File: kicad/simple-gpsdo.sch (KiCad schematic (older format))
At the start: 89 parts, among them J1 PPS_OUT, J2 PWR, J3 ISP, J6 USB_B_Micro, J7 NEO-6M, J8 10MHz_OUT, Q1 DMP3099L, SW1 RST, U1 BD50FC0FP-E2, U2 ATmega32U4-AU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

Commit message: Updated tantalum footprints, started new BOM
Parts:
- C27, C8: footprint Capacitor_SMD:C_1206_3216Metric_Pad1.42x1.75mm_HandSolder -> Capacitor_Tantalum_SMD:CP_EIA-6032-20_AVX-F_Pad2.25x2.35mm_HandSolder
- C3, C32, C34, C35: footprint Capacitor_SMD:C_1206_3216Metric_Pad1.42x1.75mm_HandSolder -> Capacitor_Tantalum_SMD:CP_EIA-3528-15_AVX-H_Pad1.50x2.35mm_HandSolder
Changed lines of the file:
@@
 F 0 "C35" H 8988 5196 50  0000 L CNN
 F 1 "10uF" H 8988 5105 50  0000 L CNN
-F 2 "Capacitor_SMD:C_1206_3216Metric_Pad1.42x1.75mm_HandSolder" H 8900 5150 50  0001 C CNN
+F 2 "Capacitor_Tantalum_SMD:CP_EIA-3528-15_AVX-H_Pad1.50x2.35mm_HandSolder" H 8900 5150 50  0001 C CNN
 F 3 "~" H 8900 5150 50  0001 C CNN
 	1    8900 5150
@@
 F 0 "C34" H 5038 4446 50  0000 L CNN
 F 1 "10uF" H 5038 4355 50  0000 L CNN
-F 2 "Capacitor_SMD:C_1206_3216Metric_Pad1.42x1.75mm_HandSolder" H 4950 4400 50  0001 C CNN
+F 2 "Capacitor_Tantalum_SMD:CP_EIA-3528-15_AVX-H_Pad1.50x2.35mm_HandSolder" H 4950 4400 50  0001 C CNN
 F 3 "~" H 4950 4400 50  0001 C CNN
 	1    4950 4400
@@
 F 0 "C3" H 2588 6996 50  0000 L CNN
 F 1 "10uF" H 2588 6905 50  0000 L CNN
-F 2 "Capacitor_SMD:C_1206_3216Metric_Pad1.42x1.75mm_HandSolder" H 2500 6950 50  0001 C CNN
+F 2 "Capacitor_Tantalum_SMD:CP_EIA-3528-15_AVX-H_Pad1.50x2.35mm_HandSolder" H 2500 6950 50  0001 C CNN
 F 3 "~" H 2500 6950 50  0001 C CNN
 	1    2500 6950
@@
 F 0 "C8" H 4088 7396 50  0000 L CNN
 F 1 "22uF" H 4088 7305 50  0000 L CNN
-F 2 "Capacitor_SMD:C_1206_3216Metric_Pad1.42x1.75mm_HandSolder" H 4000 7350 50  0001 C CNN
+F 2 "Capacitor_Tantalum_SMD:CP_EIA-6032-20_AVX-F_Pad2.25x2.35mm_HandSolder" H 4000 7350 50  0001 C CNN
 F 3 "~" H 4000 7350 50  0001 C CNN
 	1    4000 7350
@@
 F 0 "C27" H 4238 7396 50  0000 L CNN
 F 1 "22uF" H 4238 7305 50  0000 L CNN
-F 2 "Capacitor_SMD:C_1206_3216Metric_Pad1.42x1.75mm_HandSolder" H 4150 7350 50  0001 C CNN
+F 2 "Capacitor_Tantalum_SMD:CP_EIA-6032-20_AVX-F_Pad2.25x2.35mm_HandSolder" H 4150 7350 50  0001 C CNN
 F 3 "~" H 4150 7350 50  0001 C CNN
 	1    4150 7350
@@
 F 0 "C32" H 4638 7396 50  0000 L CNN
 F 1 "10uF" H 4638 7305 50  0000 L CNN
-F 2 "Capacitor_SMD:C_1206_3216Metric_Pad1.42x1.75mm_HandSolder" H 4550 7350 50  0001 C CNN
+F 2 "Capacitor_Tantalum_SMD:CP_EIA-3528-15_AVX-H_Pad1.50x2.35mm_HandSolder" H 4550 7350 50  0001 C CNN
 F 3 "~" H 4550 7350 50  0001 C CNN
 	1    4550 7350

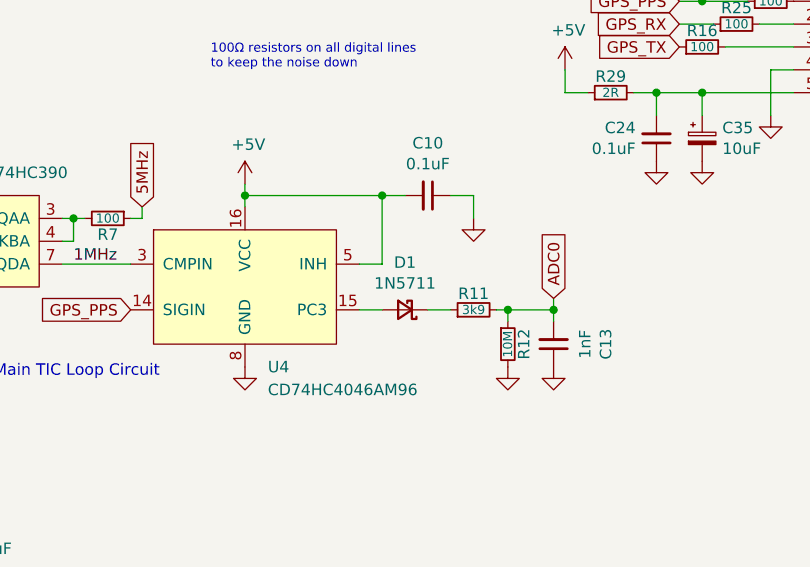
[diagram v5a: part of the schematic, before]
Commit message: Changed 1N5711 to 1N6263 for availability
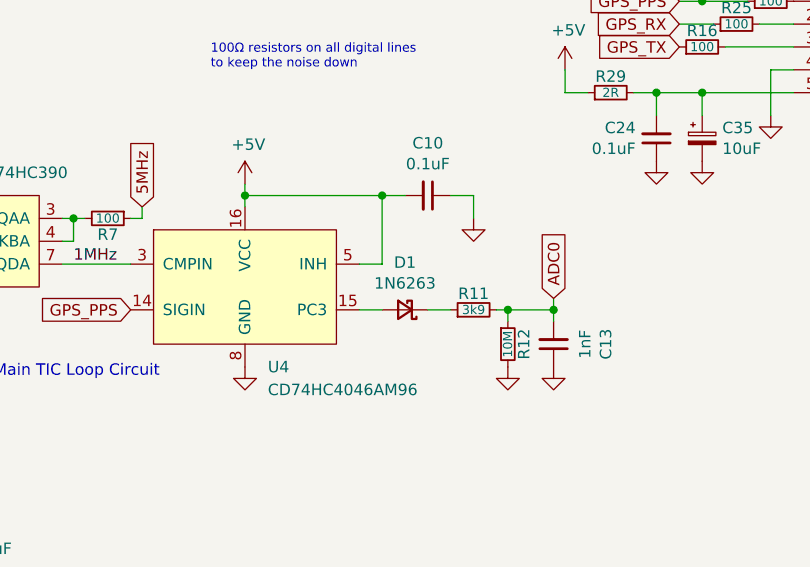
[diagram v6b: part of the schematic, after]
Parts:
- D1: value 1N5711 -> 1N6263
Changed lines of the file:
@@
 P 7600 5900
 F 0 "D1" H 7600 5693 50  0000 C CNN
-F 1 "1N5711" H 7600 5784 50  0000 C CNN
+F 1 "1N6263" H 7600 5784 50  0000 C CNN
 F 2 "Diode_SMD:D_SOD-123" V 7600 5900 50  0001 C CNN
 F 3 "~" V 7600 5900 50  0001 C CNN

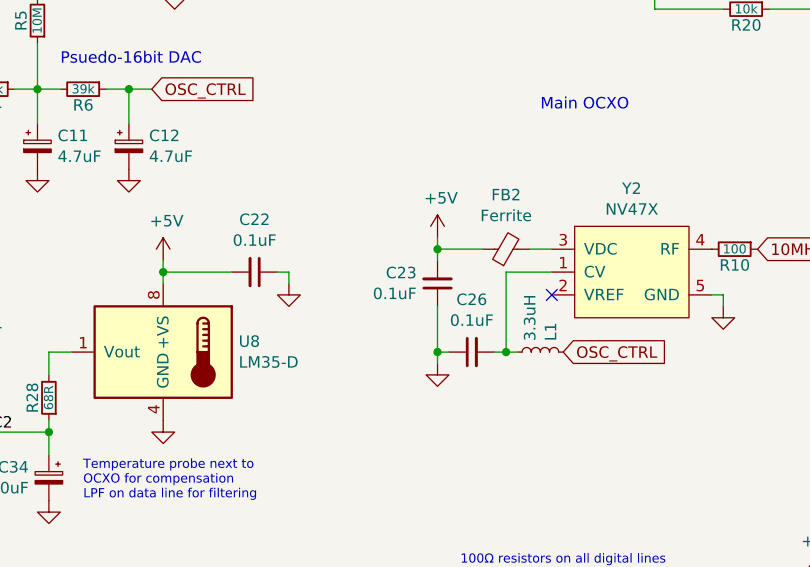
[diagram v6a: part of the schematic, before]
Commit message: Replaced C23 (0.1uF) with C14 (4.7uF)
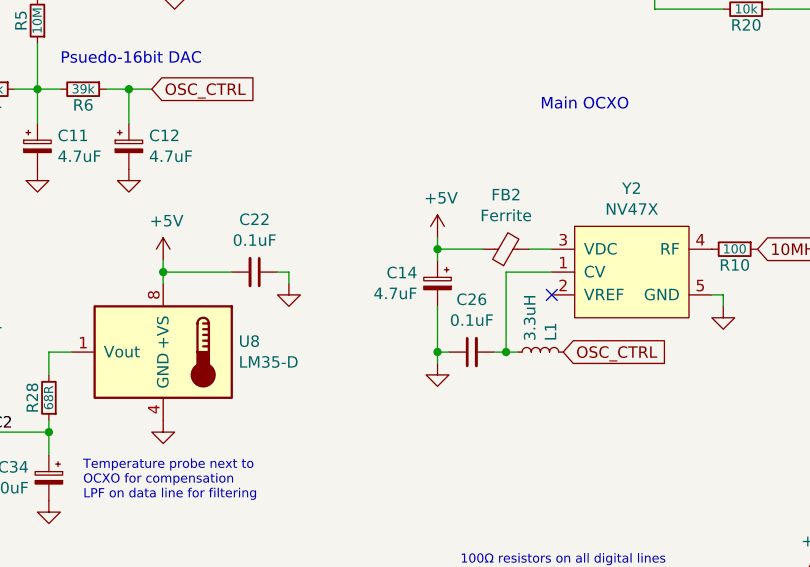
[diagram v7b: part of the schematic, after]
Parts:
- removed C23: 0.1uF, Capacitor_SMD:C_0805_2012Metric_Pad1.15x1.40mm_HandSolder, symbol Device:C_Small
- added C14: 4.7uF, Capacitor_Tantalum_SMD:CP_EIA-3216-10_Kemet-I_Pad1.58x1.35mm_HandSolder, symbol Device:CP_Small
- C11, C12, C25, C30: footprint Capacitor_SMD:C_1206_3216Metric_Pad1.42x1.75mm_HandSolder -> Capacitor_Tantalum_SMD:CP_EIA-3216-10_Kemet-I_Pad1.58x1.35mm_HandSolder
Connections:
- net +5V: now also C14.1
- net GND: now also C14.2
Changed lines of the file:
@@
 F 0 "C11" H 4988 2996 50  0000 L CNN
 F 1 "4.7uF" H 4988 2905 50  0000 L CNN
-F 2 "Capacitor_SMD:C_1206_3216Metric_Pad1.42x1.75mm_HandSolder" H 4900 2950 50  0001 C CNN
+F 2 "Capacitor_Tantalum_SMD:CP_EIA-3216-10_Kemet-I_Pad1.58x1.35mm_HandSolder" H 4900 2950 50  0001 C CNN
 F 3 "~" H 4900 2950 50  0001 C CNN
 	1    4900 2950
@@
 F 0 "C12" H 5388 2996 50  0000 L CNN
 F 1 "4.7uF" H 5388 2905 50  0000 L CNN
-F 2 "Capacitor_SMD:C_1206_3216Metric_Pad1.42x1.75mm_HandSolder" H 5300 2950 50  0001 C CNN
+F 2 "Capacitor_Tantalum_SMD:CP_EIA-3216-10_Kemet-I_Pad1.58x1.35mm_HandSolder" H 5300 2950 50  0001 C CNN
 F 3 "~" H 5300 2950 50  0001 C CNN
 	1    5300 2950
@@
 F 0 "C25" H 1638 1396 50  0000 L CNN
 F 1 "4.7uF" H 1638 1305 50  0000 L CNN
-F 2 "Capacitor_SMD:C_1206_3216Metric_Pad1.42x1.75mm_HandSolder" H 1550 1350 50  0001 C CNN
+F 2 "Capacitor_Tantalum_SMD:CP_EIA-3216-10_Kemet-I_Pad1.58x1.35mm_HandSolder" H 1550 1350 50  0001 C CNN
 F 3 "~" H 1550 1350 50  0001 C CNN
 	1    1550 1350
@@
 OSC_CTRL
 $Comp
-L Device:C_Small C23
-U 1 1 5F6CD16E
-P 6650 3550
-F 0 "C23" H 6559 3504 50  0000 R CNN
-F 1 "0.1uF" H 6559 3595 50  0000 R CNN
-F 2 "Capacitor_SMD:C_0805_2012Metric_Pad1.15x1.40mm_HandSolder" H 6650 3550 50  0001 C CNN
-F 3 "~" H 6650 3550 50  0001 C CNN
-	1    6650 3550
-	1    0    0    1
-$EndComp
-$Comp
 L power:+5V #PWR018
 U 1 1 6199610A
@@
 F 0 "C30" H 5688 6946 50  0000 L CNN
 F 1 "4.7uF" H 5688 6855 50  0000 L CNN
-F 2 "Capacitor_SMD:C_1206_3216Metric_Pad1.42x1.75mm_HandSolder" H 5600 6900 50  0001 C CNN
+F 2 "Capacitor_Tantalum_SMD:CP_EIA-3216-10_Kemet-I_Pad1.58x1.35mm_HandSolder" H 5600 6900 50  0001 C CNN
 F 3 "~" H 5600 6900 50  0001 C CNN
 	1    5600 6900
@@
 Text Notes 8850 3050 0    40   ~ 0
 PPS connection is a jumper\nto bulkhead SMA
+$Comp
+L Device:CP_Small C14
+U 1 1 61775BC3
+P 6650 3550
+F 0 "C14" H 6738 3596 50  0000 L CNN
+F 1 "4.7uF" H 6738 3505 50  0000 L CNN
+F 2 "Capacitor_Tantalum_SMD:CP_EIA-3216-10_Kemet-I_Pad1.58x1.35mm_HandSolder" H 6650 3550 50  0001 C CNN
+F 3 "~" H 6650 3550 50  0001 C CNN
+	1    6650 3550
+	-1   0    0    -1
+$EndComp
 $EndSCHEMATC

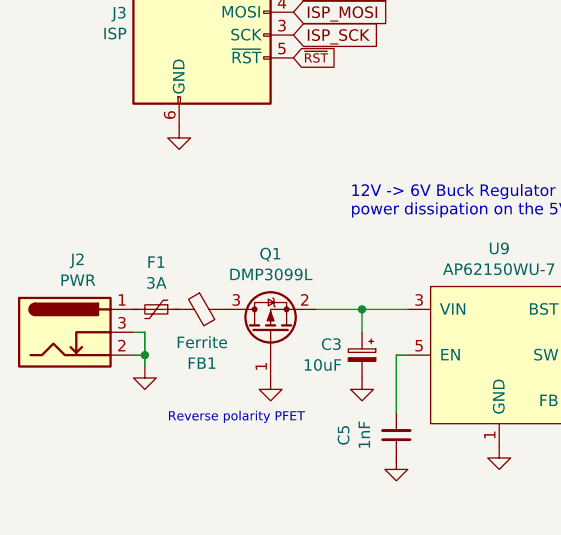
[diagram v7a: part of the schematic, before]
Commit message: Changed input fuse from 3A to 2A
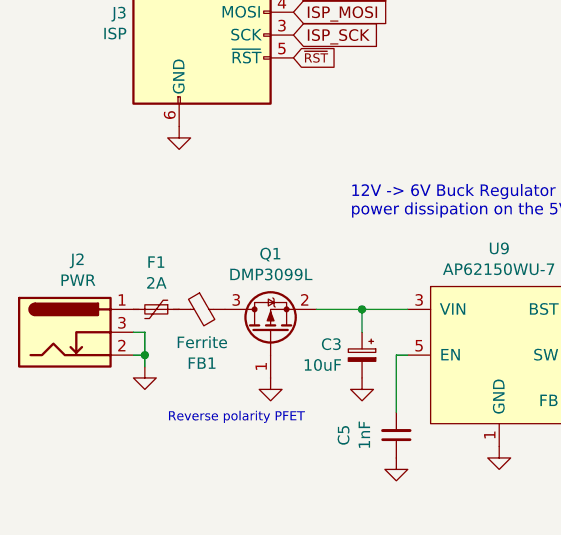
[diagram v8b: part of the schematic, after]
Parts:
- F1: value 3A -> 2A
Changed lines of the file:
@@
 P 1600 6750
 F 0 "F1" V 1395 6750 50  0000 C CNN
-F 1 "3A" V 1486 6750 50  0000 C CNN
+F 1 "2A" V 1486 6750 50  0000 C CNN
 F 2 "Fuse:Fuse_1206_3216Metric_Pad1.42x1.75mm_HandSolder" H 1650 6550 50  0001 L CNN
 F 3 "~" H 1600 6750 50  0001 C CNN
